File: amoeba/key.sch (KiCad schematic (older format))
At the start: 4 parts

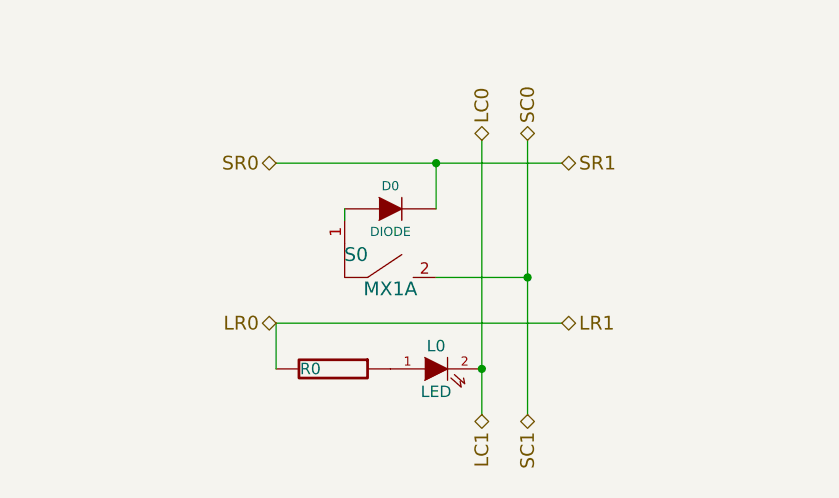
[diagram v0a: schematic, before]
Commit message: Added surface mount pads to Amoeba and bumped version number to 1.1.0.
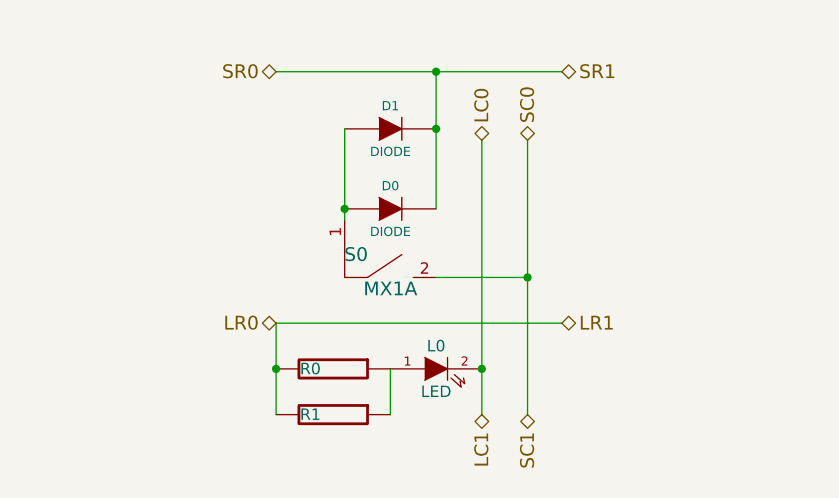
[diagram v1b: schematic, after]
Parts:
- added D1: DIODE, ~, symbol DIODE
- added R1: RESISTOR, ~, symbol RESISTOR
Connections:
- net LR0: now also R1.2
- net SR0: now also D1.2 (K)
- net at D0.1 (A), S0.1: now also D1.1 (A)
- net at L0.1 (A), R0.1: now also R1.1
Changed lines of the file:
@@
 $EndComp
 Wire Wire Line
-	5150 4200 5150 4000
+	5150 4000 5150 4400
 Connection ~ 6050 4200
 Wire Wire Line
 	5850 3800 6250 3800
 Connection ~ 6250 3800
-Connection ~ 5850 3300
 Wire Wire Line
 	6050 4400 6050 3200
@@
 	6250 3200 6250 4400
 Wire Wire Line
-	5150 3300 6400 3300
-Wire Wire Line
 	5150 4000 6400 4000
 Wire Wire Line
-	5450 3500 5450 3550
-Wire Wire Line
-	5850 3500 5850 3300
+	5450 3150 5450 3550
 Text HLabel 6250 3200 1    60   BiDi ~ 0
 SC0
 Text HLabel 6050 3200 1    60   BiDi ~ 0
 LC0
-Text HLabel 6400 3300 2    60   BiDi ~ 0
+Text HLabel 6400 2900 2    60   BiDi ~ 0
 SR1
-Text HLabel 5150 3300 0    60   BiDi ~ 0
+Text HLabel 5150 2900 0    60   BiDi ~ 0
 SR0
 Text HLabel 6400 4000 2    60   BiDi ~ 0
@@
 Text HLabel 6250 4400 3    60   BiDi ~ 0
 SC1
+$Comp
+L DIODE D1
+U 1 1 55DA9CD1
+P 5650 3150
+F 0 "D1" H 5650 3250 40  0000 C CNN
+F 1 "DIODE" H 5650 3050 40  0000 C CNN
+F 2 "~" H 5650 3150 60  0000 C CNN
+F 3 "~" H 5650 3150 60  0000 C CNN
+	1    5650 3150
+	1    0    0    -1
+$EndComp
+Wire Wire Line
+	6400 2900 5150 2900
+Wire Wire Line
+	5850 2900 5850 3500
+Connection ~ 5850 2900
+Connection ~ 5850 3150
+Connection ~ 5450 3500
+$Comp
+L RESISTOR R1
+U 1 1 55DA9D6F
+P 5400 4400
+F 0 "R1" V 5400 4300 50  0000 C CNN
+F 1 "RESISTOR" H 5400 4500 50  0001 C CNN
+F 2 "~" H 5400 4400 60  0000 C CNN
+F 3 "~" H 5400 4400 60  0000 C CNN
+	1    5400 4400
+	0    1    1    0
+$EndComp
+Wire Wire Line
+	5650 4400 5650 4200
+Connection ~ 5150 4200
 $EndSCHEMATC

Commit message: Split key schematic into multiple sheets.
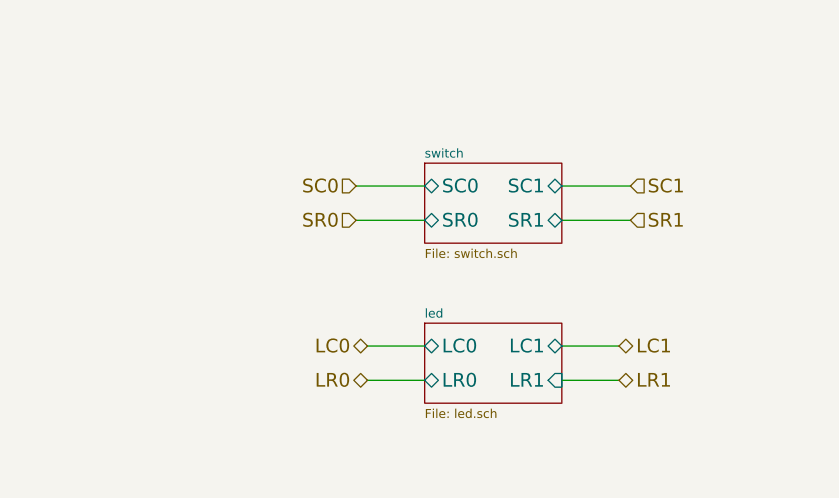
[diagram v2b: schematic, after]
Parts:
- removed D0, D1: DIODE, ~, symbol DIODE
- removed L0: LED, ~, symbol LED
- removed R0, R1: RESISTOR, ~, symbol RESISTOR
- removed S0: MX1A, ~, symbol MX1A
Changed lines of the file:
@@
 $Descr A4 11693 8268
 encoding utf-8
-Sheet 2 2
+Sheet 2 4
 Title ""
-Date "24 aug 2015"
+Date "25 aug 2015"
 Rev ""
 Comp ""
@@
 Comment4 ""
 $EndDescr
-$Comp
-L MX1A S0
-U 1 1 55D93046
-P 5650 3950
-F 0 "S0" H 5500 4200 60  0000 C CNN
-F 1 "MX1A" H 5650 4050 60  0000 C CNN
-F 2 "~" H 5650 3950 60  0000 C CNN
-F 3 "~" H 5650 3950 60  0000 C CNN
-	1    5650 3950
-	1    0    0    -1
-$EndComp
-$Comp
-L DIODE D0
-U 1 1 55D9304C
-P 5650 3500
-F 0 "D0" H 5650 3600 40  0000 C CNN
-F 1 "DIODE" H 5650 3400 40  0000 C CNN
-F 2 "~" H 5650 3500 60  0000 C CNN
-F 3 "~" H 5650 3500 60  0000 C CNN
-	1    5650 3500
-	1    0    0    -1
-$EndComp
-$Comp
-L LED L0
-U 1 1 55D93052
-P 5850 4200
-F 0 "L0" H 5850 4300 50  0000 C CNN
-F 1 "LED" H 5850 4100 50  0000 C CNN
-F 2 "~" H 5850 4200 60  0000 C CNN
-F 3 "~" H 5850 4200 60  0000 C CNN
-	1    5850 4200
-	1    0    0    -1
-$EndComp
-$Comp
-L RESISTOR R0
-U 1 1 55D93058
-P 5400 4200
-F 0 "R0" V 5400 4100 50  0000 C CNN
-F 1 "RESISTOR" H 5400 4300 50  0001 C CNN
-F 2 "~" H 5400 4200 60  0000 C CNN
-F 3 "~" H 5400 4200 60  0000 C CNN
-	1    5400 4200
-	0    1    1    0
-$EndComp
+Text HLabel 5550 4100 0    60   BiDi ~ 0
+LC0
+Text HLabel 6650 4250 2    60   BiDi ~ 0
+LR1
+Text HLabel 5550 4250 0    60   BiDi ~ 0
+LR0
+Text HLabel 6650 4100 2    60   BiDi ~ 0
+LC1
+$Sheet
+S 5800 4000 600  350
+U 55DBAE59
+F0 "led" 39
+F1 "led.sch" 39
+F2 "LC0" B L 5800 4100 60
+F3 "LR0" B L 5800 4250 60
+F4 "LC1" B R 6400 4100 60
+F5 "LR1" I R 6400 4250 60
+$EndSheet
+$Sheet
+S 5800 3300 600  350
+U 55DBAE5B
+F0 "switch" 39
+F1 "switch.sch" 39
+F2 "SC0" B L 5800 3400 60
+F3 "SR1" B R 6400 3550 60
+F4 "SR0" B L 5800 3550 60
+F5 "SC1" B R 6400 3400 60
+$EndSheet
 Wire Wire Line
-	5150 4000 5150 4400
-Connection ~ 6050 4200
+	6650 4100 6400 4100
 Wire Wire Line
-	5850 3800 6250 3800
-Connection ~ 6250 3800
+	6400 4250 6650 4250
 Wire Wire Line
-	6050 4400 6050 3200
+	5800 4250 5550 4250
 Wire Wire Line
-	6250 3200 6250 4400
+	5550 4100 5800 4100
+Text HLabel 5500 3400 0    60   Input ~ 0
+SC0
+Text HLabel 6700 3400 2    60   Input ~ 0
+SC1
+Text HLabel 6700 3550 2    60   Input ~ 0
+SR1
+Text HLabel 5500 3550 0    60   Input ~ 0
+SR0
 Wire Wire Line
-	5150 4000 6400 4000
+	6700 3400 6400 3400
 Wire Wire Line
-	5450 3150 5450 3550
-Text HLabel 6250 3200 1    60   BiDi ~ 0
-SC0
-Text HLabel 6050 3200 1    60   BiDi ~ 0
-LC0
-Text HLabel 6400 2900 2    60   BiDi ~ 0
-SR1
-Text HLabel 5150 2900 0    60   BiDi ~ 0
-SR0
-Text HLabel 6400 4000 2    60   BiDi ~ 0
-LR1
-Text HLabel 5150 4000 0    60   BiDi ~ 0
-LR0
-Text HLabel 6050 4400 3    60   BiDi ~ 0
-LC1
-Text HLabel 6250 4400 3    60   BiDi ~ 0
-SC1
-$Comp
-L DIODE D1
-U 1 1 55DA9CD1
-P 5650 3150
-F 0 "D1" H 5650 3250 40  0000 C CNN
-F 1 "DIODE" H 5650 3050 40  0000 C CNN
-F 2 "~" H 5650 3150 60  0000 C CNN
-F 3 "~" H 5650 3150 60  0000 C CNN
-	1    5650 3150
-	1    0    0    -1
-$EndComp
+	6400 3550 6700 3550
 Wire Wire Line
-	6400 2900 5150 2900
+	5800 3550 5500 3550
 Wire Wire Line
-	5850 2900 5850 3500
-Connection ~ 5850 2900
-Connection ~ 5850 3150
-Connection ~ 5450 3500
-$Comp
-L RESISTOR R1
-U 1 1 55DA9D6F
-P 5400 4400
-F 0 "R1" V 5400 4300 50  0000 C CNN
-F 1 "RESISTOR" H 5400 4500 50  0001 C CNN
-F 2 "~" H 5400 4400 60  0000 C CNN
-F 3 "~" H 5400 4400 60  0000 C CNN
-	1    5400 4400
-	0    1    1    0
-$EndComp
-Wire Wire Line
-	5650 4400 5650 4200
-Connection ~ 5150 4200
+	5500 3400 5800 3400
 $EndSCHEMATC

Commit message: Schematic clean-up.
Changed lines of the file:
@@
 Comment4 ""
 $EndDescr
-Text HLabel 5550 4100 0    60   BiDi ~ 0
+Text HLabel 5400 2950 1    60   BiDi ~ 0
 LC0
-Text HLabel 6650 4250 2    60   BiDi ~ 0
+Text HLabel 5400 3450 2    60   BiDi ~ 0
 LR1
-Text HLabel 5550 4250 0    60   BiDi ~ 0
+Text HLabel 4300 3450 0    60   BiDi ~ 0
 LR0
-Text HLabel 6650 4100 2    60   BiDi ~ 0
+Text HLabel 5400 3950 3    60   BiDi ~ 0
 LC1
 $Sheet
-S 5800 4000 600  350
+S 4550 3200 600  500
 U 55DBAE59
 F0 "led" 39
 F1 "led.sch" 39
-F2 "LC0" B L 5800 4100 60
-F3 "LR0" B L 5800 4250 60
-F4 "LC1" B R 6400 4100 60
-F5 "LR1" I R 6400 4250 60
+F2 "LC0" B R 5150 3300 60
+F3 "LR0" B L 4550 3450 60
+F4 "LC1" B R 5150 3600 60
+F5 "LR1" I R 5150 3450 60
 $EndSheet
 $Sheet
-S 5800 3300 600  350
+S 6400 3200 600  500
 U 55DBAE5B
 F0 "switch" 39
 F1 "switch.sch" 39
-F2 "SC0" B L 5800 3400 60
-F3 "SR1" B R 6400 3550 60
-F4 "SR0" B L 5800 3550 60
-F5 "SC1" B R 6400 3400 60
+F2 "SC0" B L 6400 3300 60
+F3 "SR1" B R 7000 3450 60
+F4 "SR0" B L 6400 3450 60
+F5 "SC1" B L 6400 3600 60
 $EndSheet
 Wire Wire Line
-	6650 4100 6400 4100
-Wire Wire Line
-	6400 4250 6650 4250
-Wire Wire Line
-	5800 4250 5550 4250
-Wire Wire Line
-	5550 4100 5800 4100
-Text HLabel 5500 3400 0    60   Input ~ 0
+	4550 3450 4300 3450
+Text HLabel 6100 2950 1    60   BiDi ~ 0
 SC0
-Text HLabel 6700 3400 2    60   Input ~ 0
+Text HLabel 6100 3950 3    60   BiDi ~ 0
 SC1
-Text HLabel 6700 3550 2    60   Input ~ 0
+Text HLabel 7250 3450 2    60   BiDi ~ 0
 SR1
-Text HLabel 5500 3550 0    60   Input ~ 0
+Text HLabel 6100 3450 0    60   BiDi ~ 0
 SR0
 Wire Wire Line
-	6700 3400 6400 3400
+	6400 3450 6100 3450
 Wire Wire Line
-	6400 3550 6700 3550
+	5150 3300 5400 3300
 Wire Wire Line
-	5800 3550 5500 3550
+	5400 3300 5400 2950
 Wire Wire Line
-	5500 3400 5800 3400
+	5150 3450 5400 3450
+Wire Wire Line
+	5150 3600 5400 3600
+Wire Wire Line
+	5400 3600 5400 3950
+Wire Wire Line
+	7250 3450 7000 3450
+Wire Wire Line
+	6400 3300 6100 3300
+Wire Wire Line
+	6100 3300 6100 2950
+Wire Wire Line
+	6100 3950 6100 3600
+Wire Wire Line
+	6100 3600 6400 3600
 $EndSCHEMATC
